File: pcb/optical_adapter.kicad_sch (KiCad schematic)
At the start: 18 parts, among them J1 Conn_01x06_Pin, Q1 BC847, Q2 BC847, Q3 BC857, Q4 BC817, U1 LM1117MP-3.3

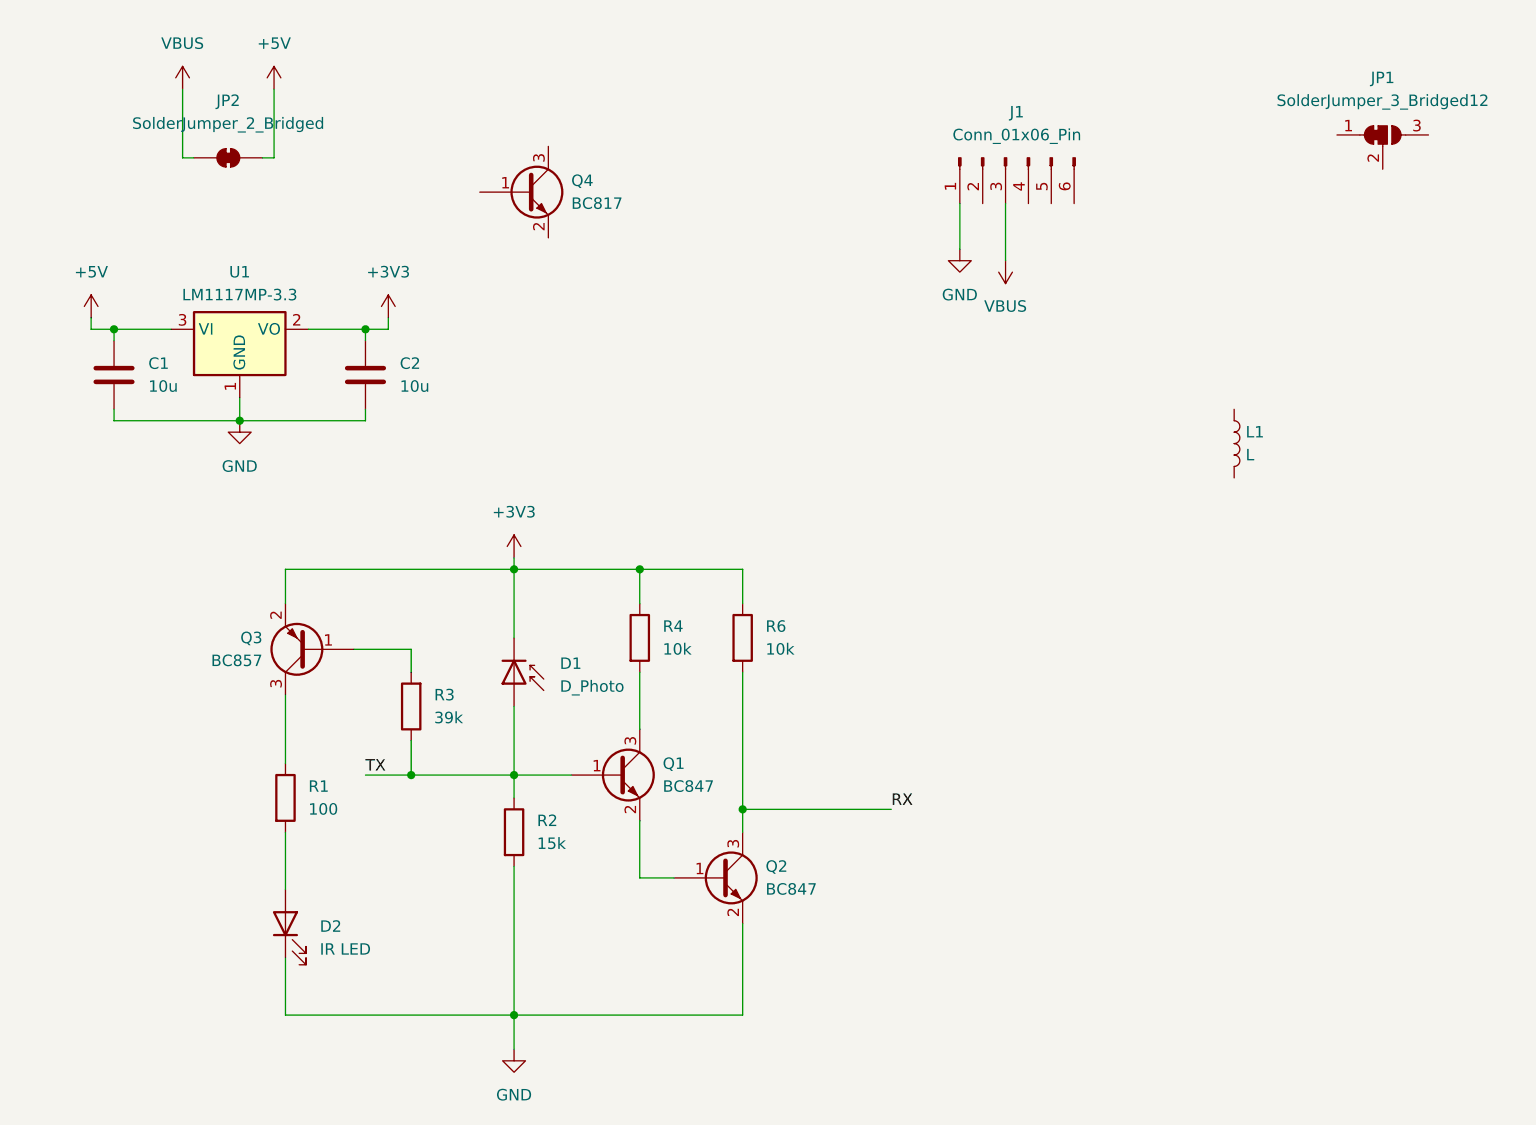
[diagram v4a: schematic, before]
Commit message: Add coil driver circuit
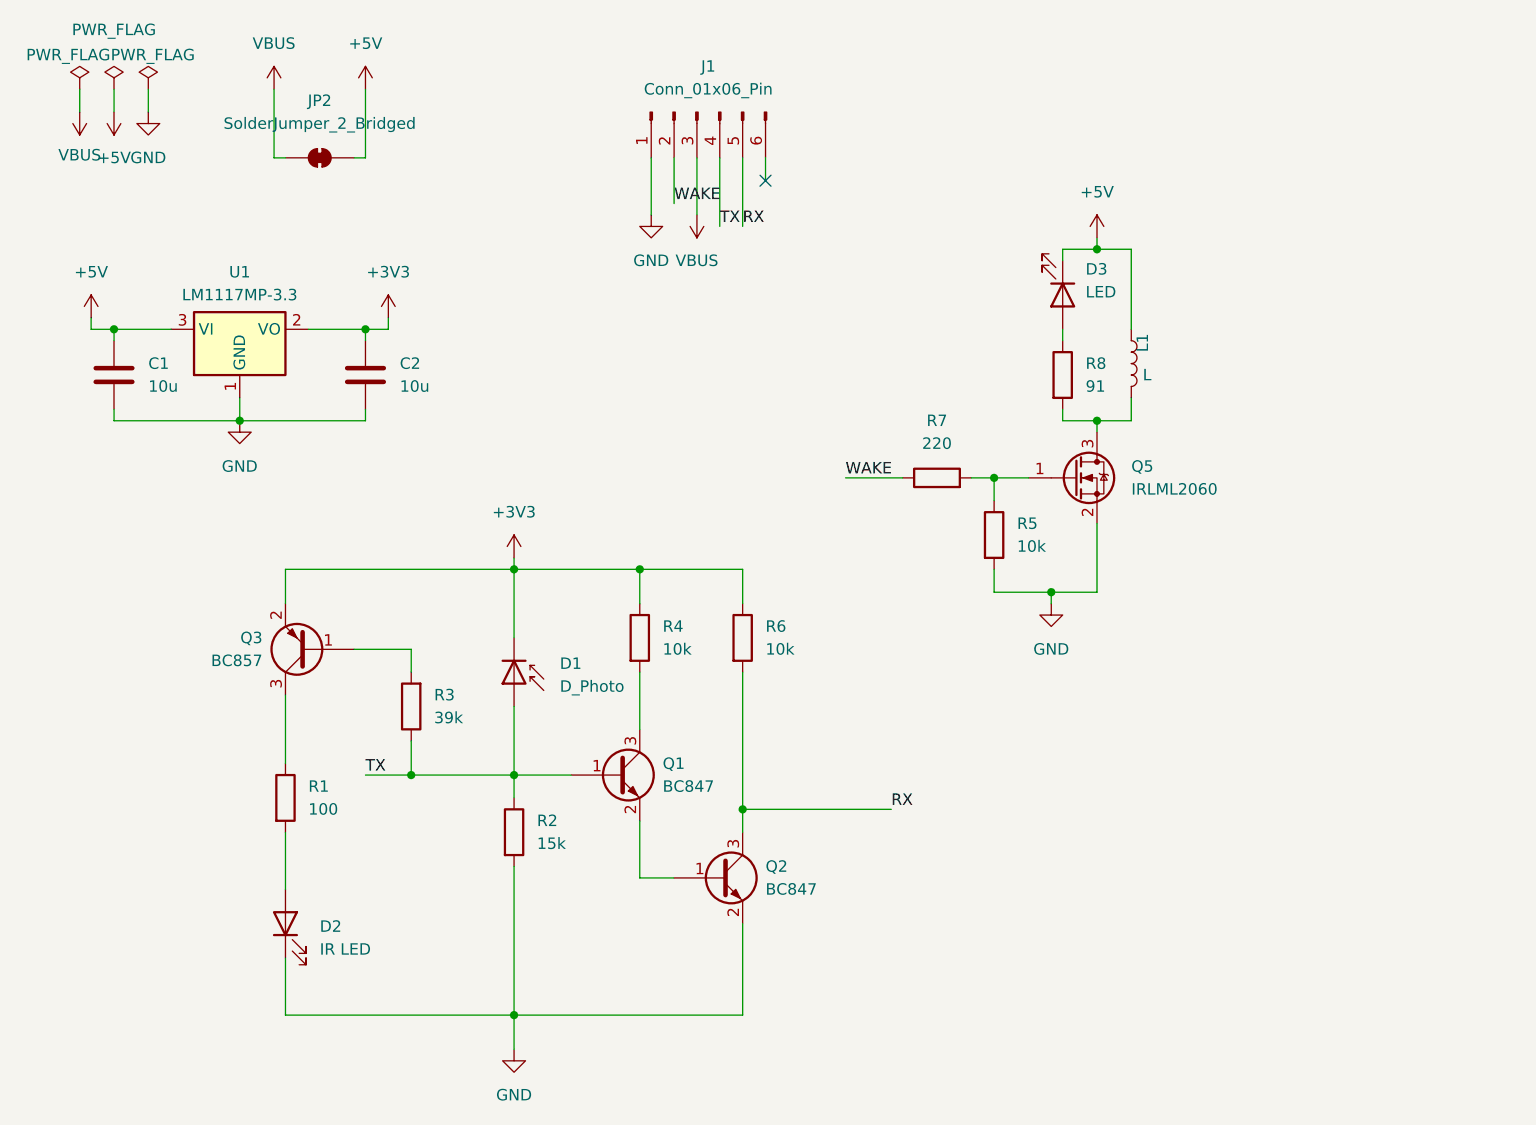
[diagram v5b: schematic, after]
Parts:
- removed JP1: SolderJumper_3_Bridged12, symbol Jumper:SolderJumper_3_Bridged12
- removed Q4: BC817, Package_TO_SOT_SMD:SOT-23, symbol Transistor_BJT:BC817
- added D3: LED, LED_SMD:LED_1206_3216Metric_Pad1.42x1.75mm_HandSolder, symbol Device:LED
- added Q5: IRLML2060, Package_TO_SOT_SMD:SOT-23, symbol Transistor_FET:IRLML2060
- added R5: 10k, Resistor_SMD:R_1206_3216Metric_Pad1.30x1.75mm_HandSolder, symbol Device:R
- added R7: 220, Resistor_SMD:R_1206_3216Metric_Pad1.30x1.75mm_HandSolder, symbol Device:R
- added R8: 91, Resistor_SMD:R_1206_3216Metric_Pad1.30x1.75mm_HandSolder, symbol Device:R
- L1: now left out of the parts list
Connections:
- net +5V: now also L1.1, D3.1 (K)
- net GND: now also Q5.2 (S), R5.2
- net RX: now also J1.5 (Pin_5)
- net TX: now also J1.4 (Pin_4)
- net WAKE: now reaches J1.2 (Pin_2)
- net WAKE: now also R7.1
- net at L1.2: now also Q5.3 (D), R8.2
- new net: Q5.1 (G), R5.1, R7.2
- new net: D3.2 (A), R8.1
- no-connect marks 0 -> 1
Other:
- title: (none) -> Multical 403 Optical Adapter
- moved on the sheet: J1, JP2, L1

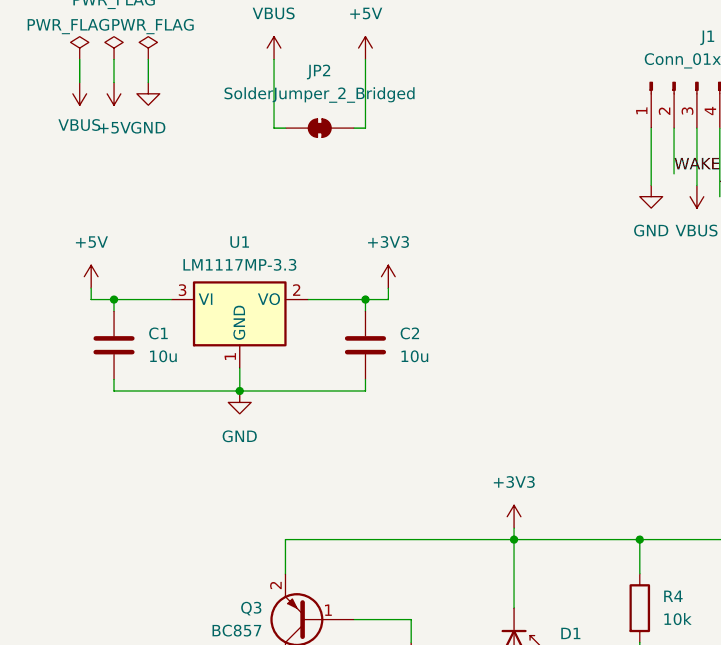
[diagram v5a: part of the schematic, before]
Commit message: Add power LED to 3V3 rail
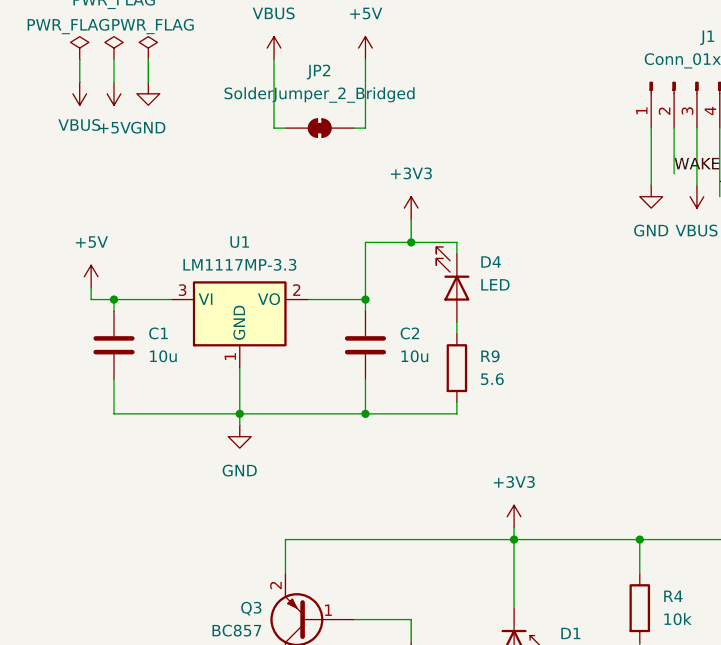
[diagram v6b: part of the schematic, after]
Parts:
- added D4: LED, LED_SMD:LED_1206_3216Metric_Pad1.42x1.75mm_HandSolder, symbol Device:LED
- added R9: 5.6, Resistor_SMD:R_1206_3216Metric_Pad1.30x1.75mm_HandSolder, symbol Device:R
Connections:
- net +3V3: now also D4.1 (K)
- net GND: now also R9.2
- new net: D4.2 (A), R9.1

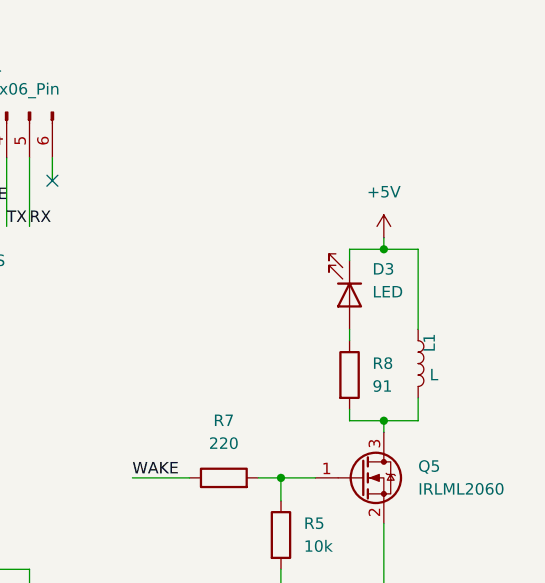
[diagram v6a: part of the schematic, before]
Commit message: Add 0 Ohms resistors to the coil
They make it possible to limit the current if needed and make
it easier to patch, e.g. change direction.
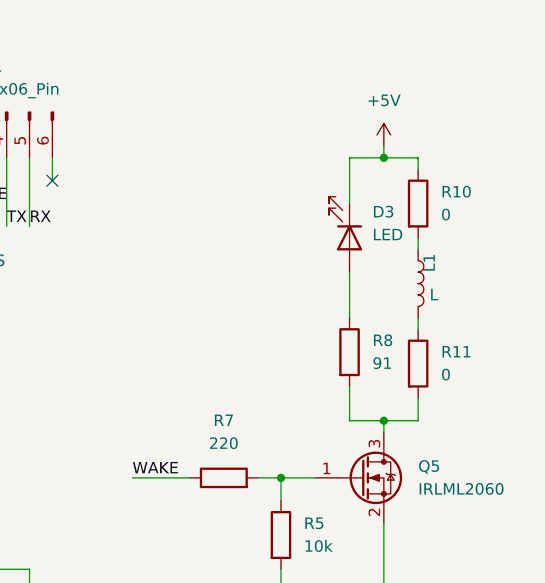
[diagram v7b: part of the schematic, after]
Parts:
- added R10, R11: 0, Resistor_SMD:R_1206_3216Metric_Pad1.30x1.75mm_HandSolder, symbol Device:R
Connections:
- net +5V: now also R10.1; no longer L1.1
- net at Q5.3 (D), R8.2: now also R11.2; no longer L1.2
- new net: L1.1, R10.2
- new net: L1.2, R11.1
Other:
- moved on the sheet: D3, L1, R8

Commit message: Remove solder bridge between VBUS and +5V
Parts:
- removed JP2: SolderJumper_2_Bridged, Jumper:SolderJumper-2_P1.3mm_Open_TrianglePad1.0x1.5mm, symbol Jumper:SolderJumper_2_Bridged
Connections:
- net VBUS is gone; now on net +5V: J1.3 (Pin_3)
